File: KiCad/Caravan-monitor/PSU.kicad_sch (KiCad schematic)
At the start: 15 parts, among them IC1 TPS54302DDCR

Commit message: Schematics done
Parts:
- removed R8: 1k, Resistor_SMD:R_0805_2012Metric_Pad1.20x1.40mm_HandSolder, symbol Device:R
- added R24: 1k, Resistor_SMD:R_0402_1005Metric_Pad0.72x0.64mm_HandSolder, symbol Device:R
- C1, C2, C3, C4, C5, C6: footprint Capacitor_SMD:C_0805_2012Metric_Pad1.18x1.45mm_HandSolder -> Capacitor_SMD:C_0402_1005Metric_Pad0.74x0.62mm_HandSolder
- D1: footprint LED_SMD:LED_0805_2012Metric_Pad1.15x1.40mm_HandSolder -> LED_SMD:LED_0402_1005Metric_Pad0.77x0.64mm_HandSolder
- R1, R2, R3, R4, R5: footprint Resistor_SMD:R_0805_2012Metric_Pad1.20x1.40mm_HandSolder -> Resistor_SMD:R_0402_1005Metric_Pad0.72x0.64mm_HandSolder
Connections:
- net GND: now also R24.2; no longer D1.1 (K)
- net Vout: now also D1.2 (A)
- new net: D1.1 (K), R24.1
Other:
- moved on the sheet: D1

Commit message: test v0.2 branch commit
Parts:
- removed IC1: TPS54302DDCR, SamacSys_Parts:SOT95P280X110-6N, symbol SamacSys_Parts:TPS54302DDCR
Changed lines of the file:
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@@
-	)
-	(symbol
-		(lib_id "SamacSys_Parts:TPS54302DDCR")
-		(at 115.57 72.39 0)
-		(unit 1)
-		(exclude_from_sim no)
-		(in_bom yes)
-		(on_board yes)
-		(dnp no)
-		(fields_autoplaced yes)
-		(property "Reference" "IC1"
-			(at 129.54 64.77 0)
-			(effects
-				(font
-					(size 1.27 1.27)
-				)
-			)
-		)
-		(property "Value" "TPS54302DDCR"
-			(at 129.54 67.31 0)
-			(effects
-				(font
-					(size 1.27 1.27)
-				)
-			)
-		)
-		(property "Footprint" "SamacSys_Parts:SOT95P280X110-6N"
-			(at 139.7 167.31 0)
-			(effects
-				(font
-					(size 1.27 1.27)
-				)
-				(justify left top)
-				(hide yes)
-			)
-		)
-		(property "Datasheet" "http://www.ti.com/general/docs/suppproductinfo.tsp?distId=10&gotoUrl=http%3A%2F%2Fwww.ti.com%2Flit%2Fgpn%2Ftps54302"
-			(at 139.7 267.31 0)
-			(effects
-				(font
-					(size 1.27 1.27)
-				)
-				(justify left top)
-				(hide yes)
-			)
-		)
-		(property "Description" "Conv DC-DC 4.5V to 28V Synchronous Step Down Single-Out 0.6V to 26V 3A 6-Pin TSOT-23 T/R"
-			(at 115.57 72.39 0)
-			(effects
-				(font
-					(size 1.27 1.27)
-				)
-				(hide yes)
-			)
-		)
-		(property "Height" "1.1"
-			(at 139.7 467.31 0)
-			(effects
-				(font
-					(size 1.27 1.27)
-				)
-				(justify left top)
-				(hide yes)
-			)
-		)
-		(property "Mouser Part Number" "595-TPS54302DDCR"
-			(at 139.7 567.31 0)
-			(effects
-				(font
-					(size 1.27 1.27)
-				)
-				(justify left top)
-				(hide yes)
-			)
-		)
-		(property "Mouser Price/Stock" "https://www.mouser.co.uk/ProductDetail/Texas-Instruments/TPS54302DDCR?qs=zEmsApcVOkUXM7UP0GSO2g%3D%3D"
-			(at 139.7 667.31 0)
-			(effects
-				(font
-					(size 1.27 1.27)
-				)
-				(justify left top)
-				(hide yes)
-			)
-		)
-		(property "Manufacturer_Name" "Texas Instruments"
-			(at 139.7 767.31 0)
-			(effects
-				(font
-					(size 1.27 1.27)
-				)
-				(justify left top)
-				(hide yes)
-			)
-		)
-		(property "Manufacturer_Part_Number" "TPS54302DDCR"
-			(at 139.7 867.31 0)
-			(effects
-				(font
-					(size 1.27 1.27)
-				)
-				(justify left top)
-				(hide yes)
-			)
-		)
-		(pin "2"
-		)
-		(pin "5"
-		)
-		(pin "3"
-		)
-		(pin "6"
-		)
-		(pin "4"
-		)
-		(pin "1"
-		)
-		(instances
-			(project ""
-				(path "/4b94aa5f-1c73-4d2e-8117-e53a25103462/ab3579b6-0764-406b-a3c2-b2926f9506eb"
-					(reference "IC1")
-					(unit 1)
-				)
-			)
-		)
 	)
 	(symbol

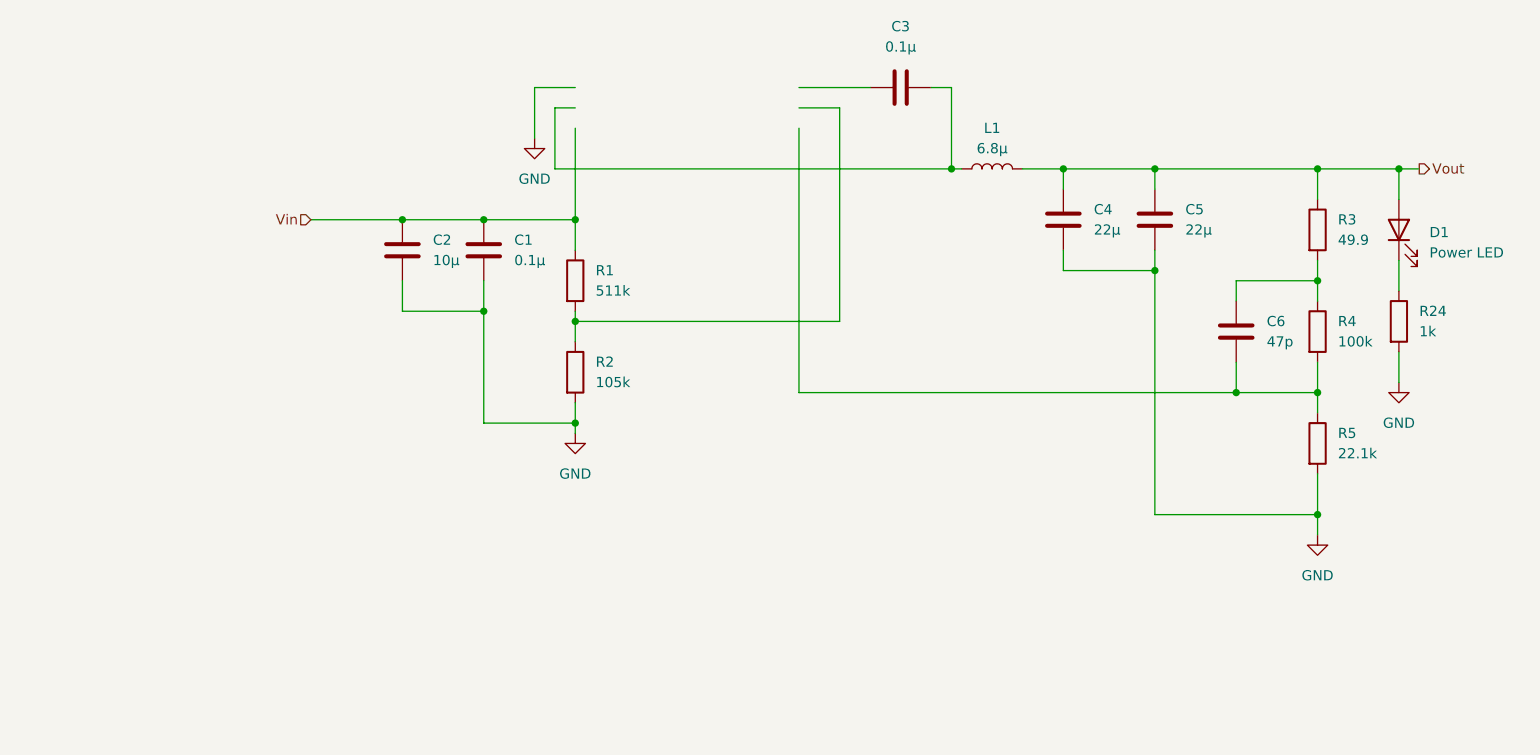
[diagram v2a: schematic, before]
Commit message: Schematic updates
Parts changed for JLCPCB assembly compatibility
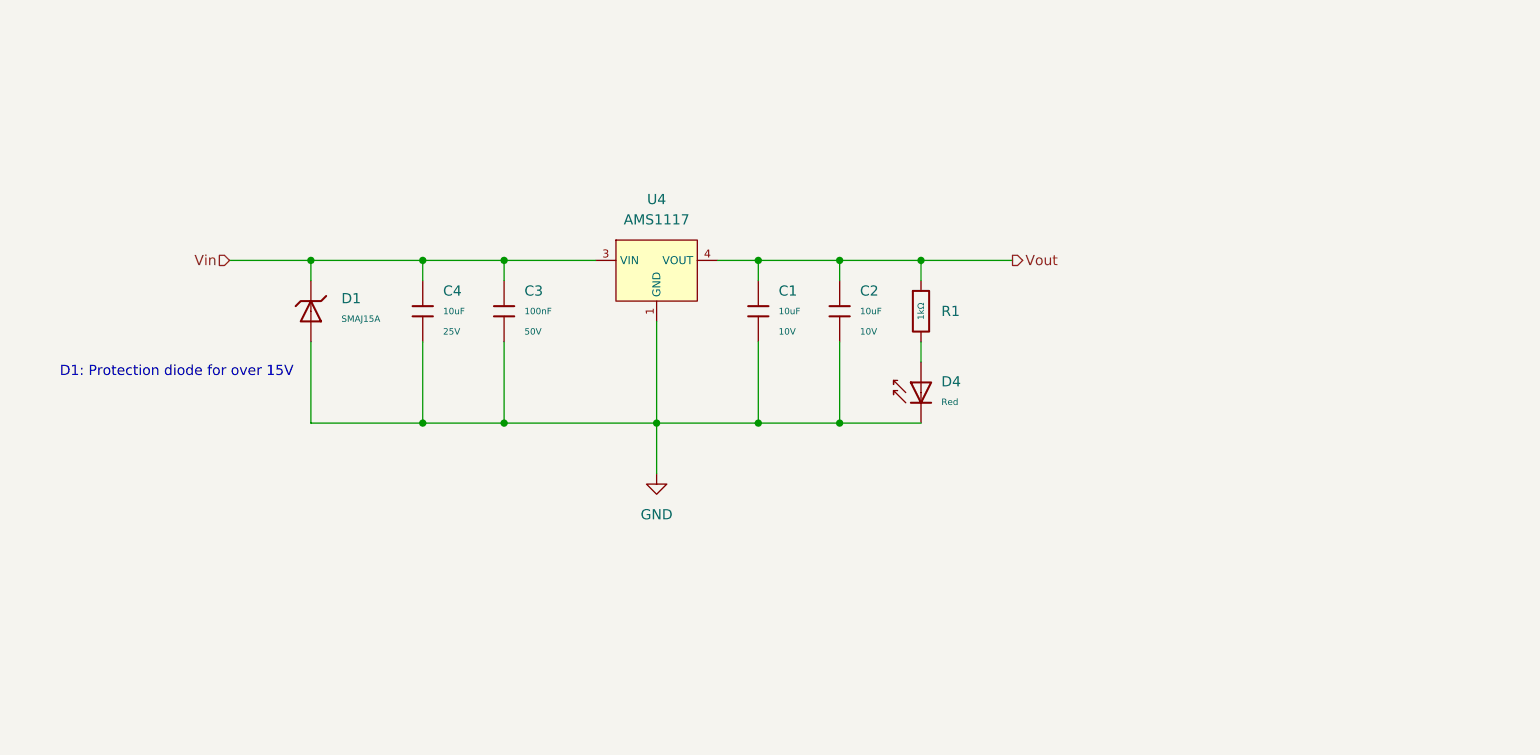
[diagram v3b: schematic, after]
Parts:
- removed C1, C3: 0.1µ, Capacitor_SMD:C_0402_1005Metric_Pad0.74x0.62mm_HandSolder, symbol Device:C
- removed C2: 10µ, Capacitor_SMD:C_0402_1005Metric_Pad0.74x0.62mm_HandSolder, symbol Device:C
- removed C4, C5: 22µ, Capacitor_SMD:C_0402_1005Metric_Pad0.74x0.62mm_HandSolder, symbol Device:C
- removed C6: 47p, Capacitor_SMD:C_0402_1005Metric_Pad0.74x0.62mm_HandSolder, symbol Device:C
- removed D1: Power LED, LED_SMD:LED_0402_1005Metric_Pad0.77x0.64mm_HandSolder, symbol Device:LED
- removed L1: 6.8µ, Inductor_SMD:L_0805_2012Metric_Pad1.05x1.20mm_HandSolder, symbol Device:L
- removed R1: 511k, Resistor_SMD:R_0402_1005Metric_Pad0.72x0.64mm_HandSolder, symbol Device:R
- removed R2: 105k, Resistor_SMD:R_0402_1005Metric_Pad0.72x0.64mm_HandSolder, symbol Device:R
- removed R24: 1k, Resistor_SMD:R_0402_1005Metric_Pad0.72x0.64mm_HandSolder, symbol Device:R
- removed R3: 49.9, Resistor_SMD:R_0402_1005Metric_Pad0.72x0.64mm_HandSolder, symbol Device:R
- removed R4: 100k, Resistor_SMD:R_0402_1005Metric_Pad0.72x0.64mm_HandSolder, symbol Device:R
- removed R5: 22.1k, Resistor_SMD:R_0402_1005Metric_Pad0.72x0.64mm_HandSolder, symbol Device:R
- added C1, C2: 10uF, PCM_JLCPCB:C_0603, symbol PCM_JLCPCB-Capacitors:0603,10uF
- added C3: 100nF, PCM_JLCPCB:C_0603, symbol PCM_JLCPCB-Capacitors:0603,100nF
- added C4: 10uF, PCM_JLCPCB:C_0805, symbol PCM_JLCPCB-Capacitors:0805,10uF
- added D1: SMAJ15A, PCM_JLCPCB:D_SMA, symbol PCM_JLCPCB-Diodes:TVS-Uni,SMAJ15A
- added D4: Red, PCM_JLCPCB:D_0603, symbol PCM_JLCPCB-Diodes:LED,0603,Red
- added R1: 1kΩ, PCM_JLCPCB:R_0402, symbol PCM_JLCPCB-Resistors:0402,1kΩ
- added U4: AMS1117, PCM_JLCPCB:SOT-223-3_L6.5-W3.4-P2.30-LS7.0-BR, symbol PCM_JLCPCB-Power:LDO, 3.3V, 1A
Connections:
- net GND: now also C1.2, C2.2, C3.2, C4.2, D1.2, D4.1, U4.1 (GND)
- net Vin: now also C3.1, C4.1, D1.1, U4.3 (VIN)
- net Vout: now also C1.1, C2.1, R1.1, U4.2 (VOUT), U4.4 (VOUT)
- new net: D4.2, R1.2
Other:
- note added: "D1: Protection diode for over 15V"

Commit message: 12V to 3.3V converter done
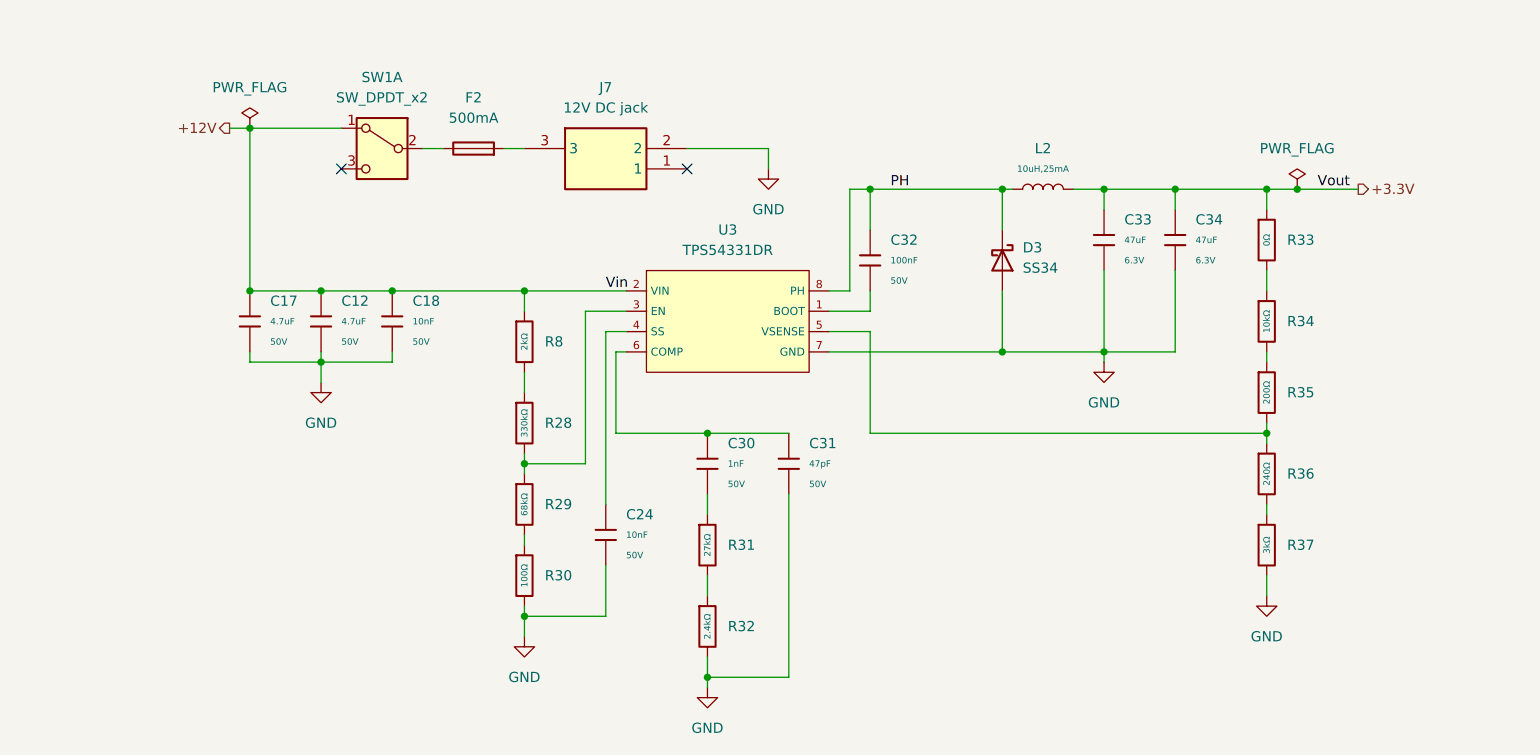
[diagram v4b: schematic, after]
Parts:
- removed C1, C2: 10uF, PCM_JLCPCB:C_0603, symbol PCM_JLCPCB-Capacitors:0603,10uF
- removed C3: 100nF, PCM_JLCPCB:C_0603, symbol PCM_JLCPCB-Capacitors:0603,100nF
- removed C4: 10uF, PCM_JLCPCB:C_0805, symbol PCM_JLCPCB-Capacitors:0805,10uF
- removed D1: SMAJ15A, PCM_JLCPCB:D_SMA, symbol PCM_JLCPCB-Diodes:TVS-Uni,SMAJ15A
- removed D4: Red, PCM_JLCPCB:D_0603, symbol PCM_JLCPCB-Diodes:LED,0603,Red
- removed R1: 1kΩ, PCM_JLCPCB:R_0402, symbol PCM_JLCPCB-Resistors:0402,1kΩ
- removed U4: AMS1117, PCM_JLCPCB:SOT-223-3_L6.5-W3.4-P2.30-LS7.0-BR, symbol PCM_JLCPCB-Power:LDO, 3.3V, 1A
- added C12, C17: 4.7uF, PCM_JLCPCB:C_1206, symbol PCM_JLCPCB-Capacitors:1206,4.7uF
- added C18: 10nF, PCM_JLCPCB:C_1206, symbol PCM_JLCPCB-Capacitors:1206,10nF
- added C24: 10nF, PCM_JLCPCB:C_0402, symbol PCM_JLCPCB-Capacitors:0402,10nF
- added C30: 1nF, PCM_JLCPCB:C_0402, symbol PCM_JLCPCB-Capacitors:0402,1nF
- added C31: 47pF, PCM_JLCPCB:C_0402, symbol PCM_JLCPCB-Capacitors:0402,47pF
- added C32: 100nF, PCM_JLCPCB:C_0805, symbol PCM_JLCPCB-Capacitors:0805,100nF,(2)
- added C33, C34: 47uF, PCM_JLCPCB:C_0805, symbol PCM_JLCPCB-Capacitors:0805,47uF
- added D3: SS34, Diode_SMD:D_SMA, symbol Diode:SS34
- added F2: 500mA, Fuse:Fuseholder_Clip-5x20mm_Littelfuse_111_Lateral_P18.80x5.00mm_D1.17mm_Horizontal, symbol Device:Fuse
- added J7: 12V DC jack, SamacSys_Parts:PJ059A, symbol SamacSys_Parts:PJ-059A
- added L2: 10uH,25mA, PCM_JLCPCB:L_1206, symbol PCM_JLCPCB-Inductors:10uH,25mA
- added R28: 330kΩ, PCM_JLCPCB:R_0805, symbol PCM_JLCPCB-Resistors:0805,330kΩ
- added R29: 68kΩ, PCM_JLCPCB:R_0805, symbol PCM_JLCPCB-Resistors:0805,68kΩ
- added R30: 100Ω, PCM_JLCPCB:R_0805, symbol PCM_JLCPCB-Resistors:0805,100Ω
- added R31: 27kΩ, PCM_JLCPCB:R_0805, symbol PCM_JLCPCB-Resistors:0805,27kΩ
- added R32: 2.4kΩ, PCM_JLCPCB:R_0805, symbol PCM_JLCPCB-Resistors:0805,2.4kΩ
- added R33: 0Ω, PCM_JLCPCB:R_0805, symbol PCM_JLCPCB-Resistors:0805,0Ω
- added R34: 10kΩ, PCM_JLCPCB:R_0805, symbol PCM_JLCPCB-Resistors:0805,10kΩ
- added R35: 200Ω, PCM_JLCPCB:R_0805, symbol PCM_JLCPCB-Resistors:0805,200Ω
- added R36: 240Ω, PCM_JLCPCB:R_0805, symbol PCM_JLCPCB-Resistors:0805,240Ω
- added R37: 3kΩ, PCM_JLCPCB:R_0805, symbol PCM_JLCPCB-Resistors:0805,3kΩ
- added R8: 2kΩ, PCM_JLCPCB:R_0805, symbol PCM_JLCPCB-Resistors:0805,2kΩ
- added SW1: SW_DPDT_x2, Button_Switch_THT:SW_E-Switch_EG2219_DPDT_Angled, symbol Switch:SW_DPDT_x2
- added U3: TPS54331DR, PCM_JLCPCB:SOIC-8_L5.0-W4.0-P1.27-LS6.0-BL, symbol PCM_JLCPCB-Power:DC-DC, Buck, 3.5-28VIN, 3A, 0.8+VOUT
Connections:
- net GND: now also C12.2, C17.2, C18.2, C24.2, C31.2, C33.2, C34.2, D3.2 (A), J7.2, R30.2, R32.2, R37.2, U3.7 (GND)
- new net: C30.2, R31.1
- new net: R31.2, R32.1
- new net: R33.2, R34.1
- new net: R34.2, R35.1
- new net: R36.2, R37.1
- new net: C24.1, U3.4 (SS)
- new net: R28.1, R8.2
- new net: C32.2, U3.1 (BOOT)
- new net: R28.2, R29.1, U3.3 (EN)
- new net: R35.2, R36.1, U3.5 (VSENSE)
- new net: C30.1, C31.1, U3.6 (COMP)
- new net: F2.1, SW1.2 (B)
- new net: F2.2, J7.3
- new net: R29.2, R30.1
- new net +12V: C12.1, C17.1, C18.1, R8.1, SW1.1 (A), U3.2 (VIN)
- new net +3.3V: C33.1, C34.1, L2.2, R33.1
- new net PH: C32.1, D3.1 (K), L2.1, U3.8 (PH)
- no-connect marks 0 -> 2
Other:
- note removed: "D1: Protection diode for over 15V"

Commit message: V0.2 PCB complete
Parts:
- removed F2: 500mA, Fuse:Fuseholder_Clip-5x20mm_Littelfuse_111_Lateral_P18.80x5.00mm_D1.17mm_Horizontal, symbol Device:Fuse
- removed J7: 12V DC jack, SamacSys_Parts:PJ059A, symbol SamacSys_Parts:PJ-059A
- removed L2: 10uH,25mA, PCM_JLCPCB:L_1206, symbol PCM_JLCPCB-Inductors:10uH,25mA
- removed SW1: SW_DPDT_x2, Button_Switch_THT:SW_E-Switch_EG2219_DPDT_Angled, symbol Switch:SW_DPDT_x2
- added D1: Red, PCM_JLCPCB:D_0805, symbol PCM_JLCPCB-Diodes:LED,0805,Red
- added DC1: DC-005-A250, EasyEDA:DC-IN-TH_DC-005-A250, symbol EasyEDA:DC-005-A250
- added FH1: 64600001003, EasyEDA:64600001003, symbol EasyEDA:64600001003
- added L1: FXL0630-6R8-M, EasyEDA:IND-SMD_L7.0-W6.6, symbol EasyEDA:FXL0630-6R8-M
- added R14: 1kΩ, PCM_JLCPCB:R_0402, symbol PCM_JLCPCB-Resistors:0402,1kΩ
- added U9: SS-12M12G5, EasyEDA:SW-TH_SS-12M12G5, symbol EasyEDA:SS-12M12G5
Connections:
- net +12V: now also U9.3
- net +3.3V: now also D1.2, L1.2
- net GND: now also DC1.2, DC1.3, R14.2
- net PH: now also L1.1
- new net: D1.1, R14.1
- new net Battery 12V: DC1.1, FH1.2
- new net Battery 12V fused: FH1.1, U9.2
- no-connect marks 2 -> 1
